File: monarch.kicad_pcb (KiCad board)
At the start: 2 copper layers, 165.4 x 129.6 mm, 140 parts, among them J1 USB_C_Receptacle_USB2.0, J2 USB_C_Receptacle_USB2.0, J3 OLED, SW1 SW_PUSH, SW10 SW_PUSH, SW11 SW_PUSH, SW12 SW_PUSH, SW13 SW_PUSH, SW14 SW_PUSH, SW15 SW_PUSH, SW16 SW_PUSH, SW17 SW_PUSH, SW18 SW_PUSH, SW19 Rotary_Encoder, SW2 SW_PUSH, SW20 SW_PUSH, SW21 SW_PUSH, SW22 SW_PUSH, SW23 SW_PUSH, SW24 SW_PUSH, SW3 SW_PUSH, SW4 SW_PUSH, SW5 SW_PUSH, SW6 SW_PUSH, SW7 SW_PUSH, SW8 SW_PUSH, SW9 SW_PUSH, U1 ATMEGA32U4, U2 MIC5219-5.0YMM

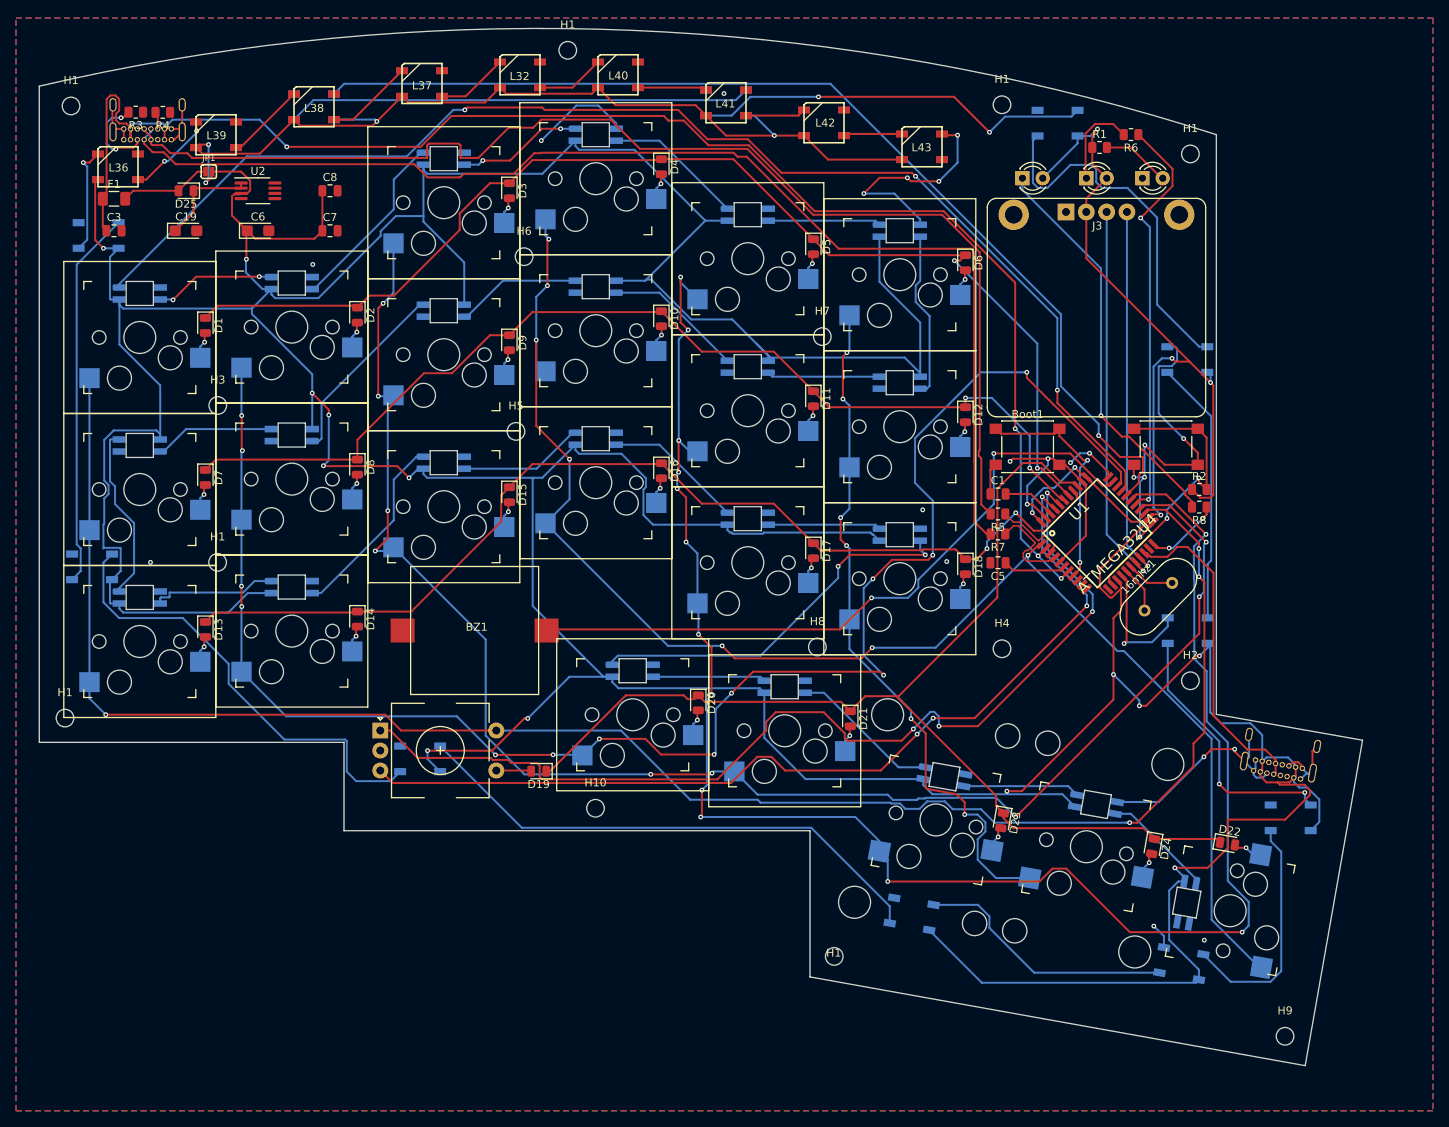
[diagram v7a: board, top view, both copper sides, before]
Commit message: logo and updating JLB components
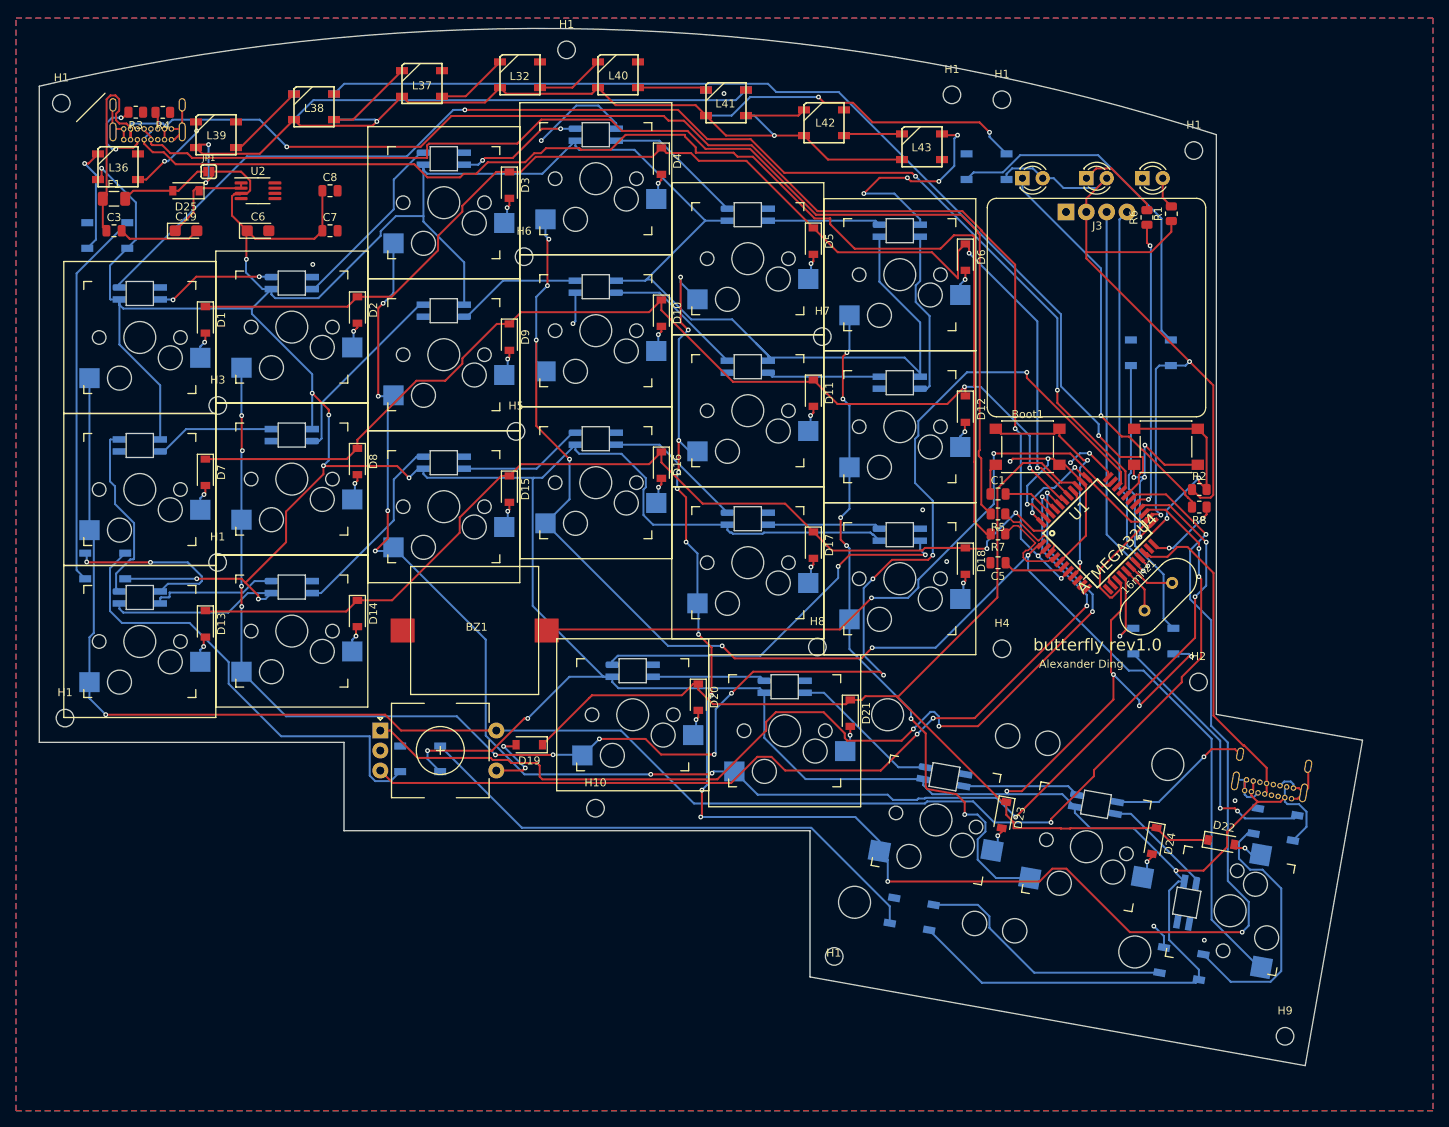
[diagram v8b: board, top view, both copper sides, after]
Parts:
- removed the H1 at (155.6, 20.4)
- removed the H1 at (15.6, 14.4)
- removed the H1 at (77.7, 7.44)
- added G***: LOGO, private:butterfly, F.Cu at (34.8, 29.7)
- added H1: Hole, MountingHole:MountingHole_2.2mm_M2, F.Cu at (125.7, 13.0)
- added H1: Hole, MountingHole:MountingHole_2.2mm_M2, F.Cu at (156.0, 20.0)
- added H1: Hole, MountingHole:MountingHole_2.2mm_M2, F.Cu at (14.4, 14.1)
- added H1: Hole, MountingHole:MountingHole_2.2mm_M2, F.Cu at (77.6, 7.39)
- D1, D10, D11, D12, D13, D14, D15, D16, D17, D18, D19, D2, D20, D21, D22, D23, D24, D25, D3, D4, D5, D6, D7, D8, D9: footprint Diode_SMD:D_0805_2012Metric -> Diode_SMD:D_SOD-123
- moved R1 12.2 mm to (153.2, 27.9), turned to 90 degrees
- moved R6 10.5 mm to (150.1, 28.3), turned to 90 degrees
- moved L3 10.4 mm to (130.1, 22.0)
- moved L4 4.63 mm to (150.6, 45.2)
- moved L5 4.50 mm to (150.9, 81.3)
- moved D19 3.50 mm to (72.9, 94.2)
- moved J2 2.71 mm to (162.3, 100.0)
- moved L6 2.08 mm to (166.2, 104.2), turned to 350 degrees
- moved L34 1.64 mm to (19.9, 71.9)
- moved L35 1.08 mm to (20.2, 30.6)
- moved H2 1.02 mm to (156.6, 86.4)
- moved D22 0.80 mm to (159.4, 106.4)
- moved D23 0.73 mm to (132.2, 103.0)
- moved D24 0.70 mm to (151.0, 106.3)
- moved D1 0.70 mm to (32.4, 41.1)
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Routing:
- net Net-(R6-Pad1): track 51.5 -> 36.6 mm
- net Net-(L2-Pad1): track 50.4 -> 41.8 mm
- net GND: track 198.4 -> 205.8 mm, vias 25 -> 26
- net COL0: track 225.6 -> 218.9 mm
- net VCC: track 980.5 -> 974.7 mm
- net Net-(J1-PadA6): track 150.5 -> 156.1 mm
- net A2: track 146.8 -> 152.3 mm
- net Net-(D19-Pad2): track 4.39 -> 9.24 mm, vias 0 -> 2
- net Net-(R1-Pad2): track 8.57 -> 3.98 mm
- net Net-(L6-Pad1): track 29.8 -> 33.2 mm
- net A3: track 130.8 -> 133.6 mm
- net Net-(L4-Pad1): track 33.1 -> 35.3 mm
- net A0: track 142.7 -> 140.9 mm
- net Net-(L3-Pad1): track 46.1 -> 44.6 mm
- net UVCC: track 193.9 -> 195.3 mm
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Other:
- board text added: "Alexander Ding"
